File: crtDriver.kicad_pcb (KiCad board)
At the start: 2 copper layers, 29 parts, among them J1 Lum_In, J2 V_Sync, J3 H_Sync, Q1 2N7000, Q2 2N7000, Q3 2N7000, Q4 2N7000

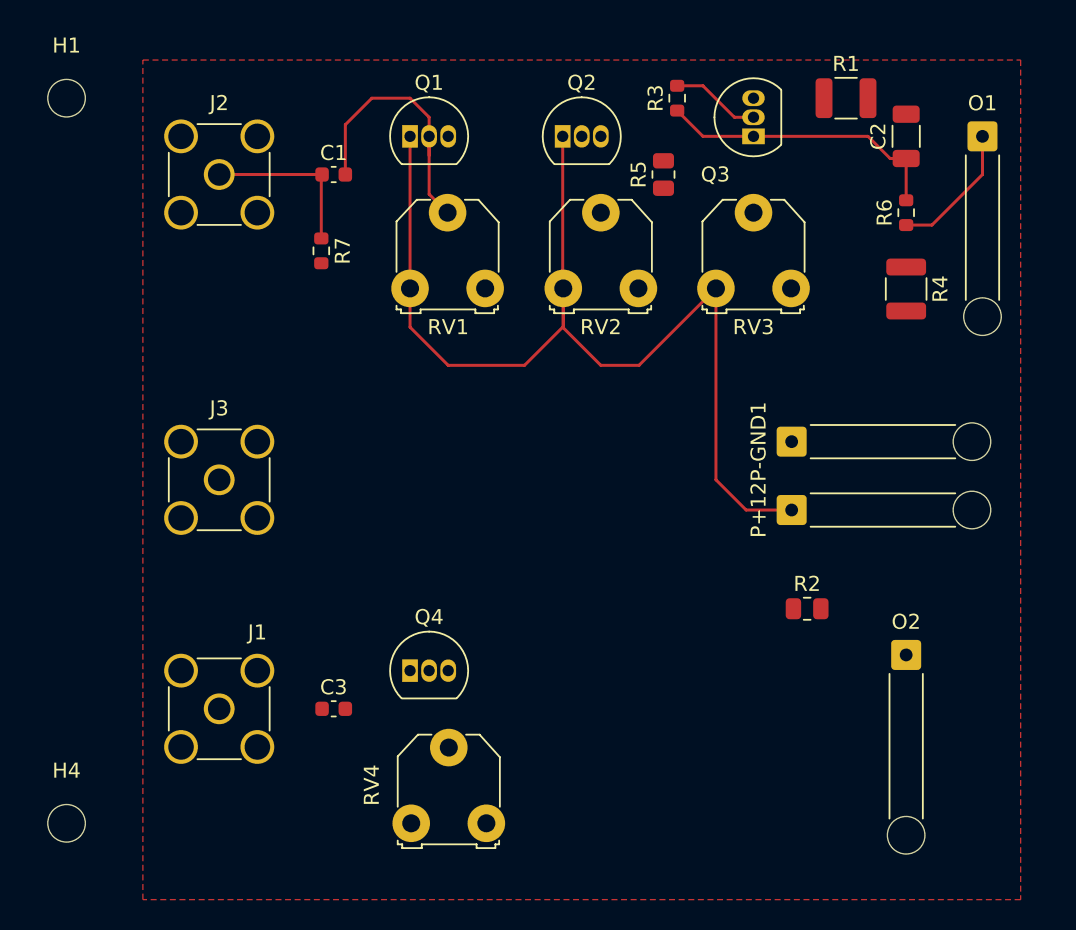
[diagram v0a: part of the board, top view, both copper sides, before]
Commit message: changed circuit to use 2n7000's as low side switches/valves to get voltage gain, started on current mirror for linear capacitor voltage ramp (it also will likely only work on the low side maybe requiring inverting of the fill/drain modes/roles, fixed luminosity amplifier design by also using mosfet on low(-) side of a resistor to boost the voltage of the input signal
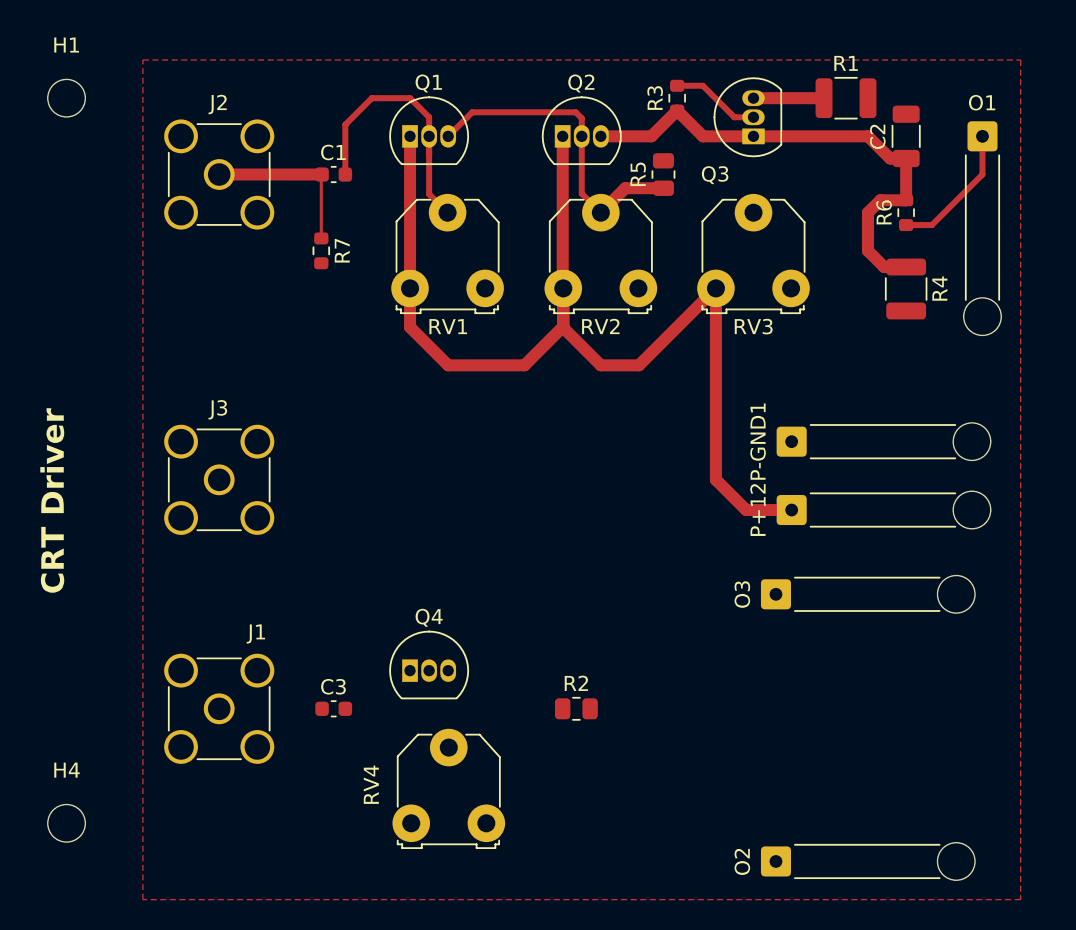
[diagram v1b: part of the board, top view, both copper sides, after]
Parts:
- added O3: V_Ramp_Out, Connector_Wire:SolderWire-0.25sqmm_1x01_D0.65mm_OD2mm_Relief, F.Cu at (151.4, 53.3)
- moved R2 16.7 mm to (138.1, 61.0)
- moved O2 16.2 mm to (151.4, 71.1), turned to 90 degrees
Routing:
- net Net-(Q1-D): track 0.00 -> 21.4 mm
- net Net-(Q2-D): track 19.3 -> 33.5 mm
- net Net-(Q3-D): track 0.00 -> 4.69 mm
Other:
- board text added: "CRT Driver"

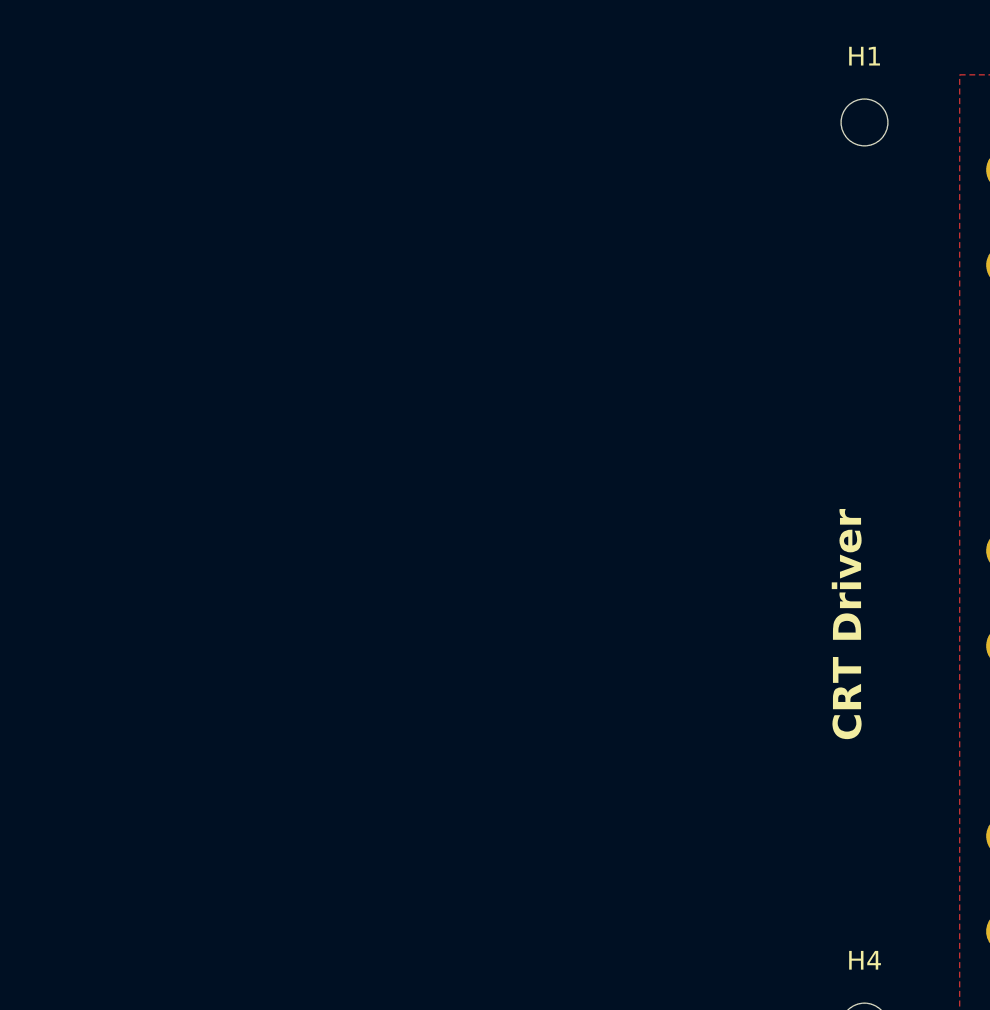
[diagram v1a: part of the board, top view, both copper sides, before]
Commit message: duplicated v sync section for h sync, adjusted luminosity amplifier passive component values
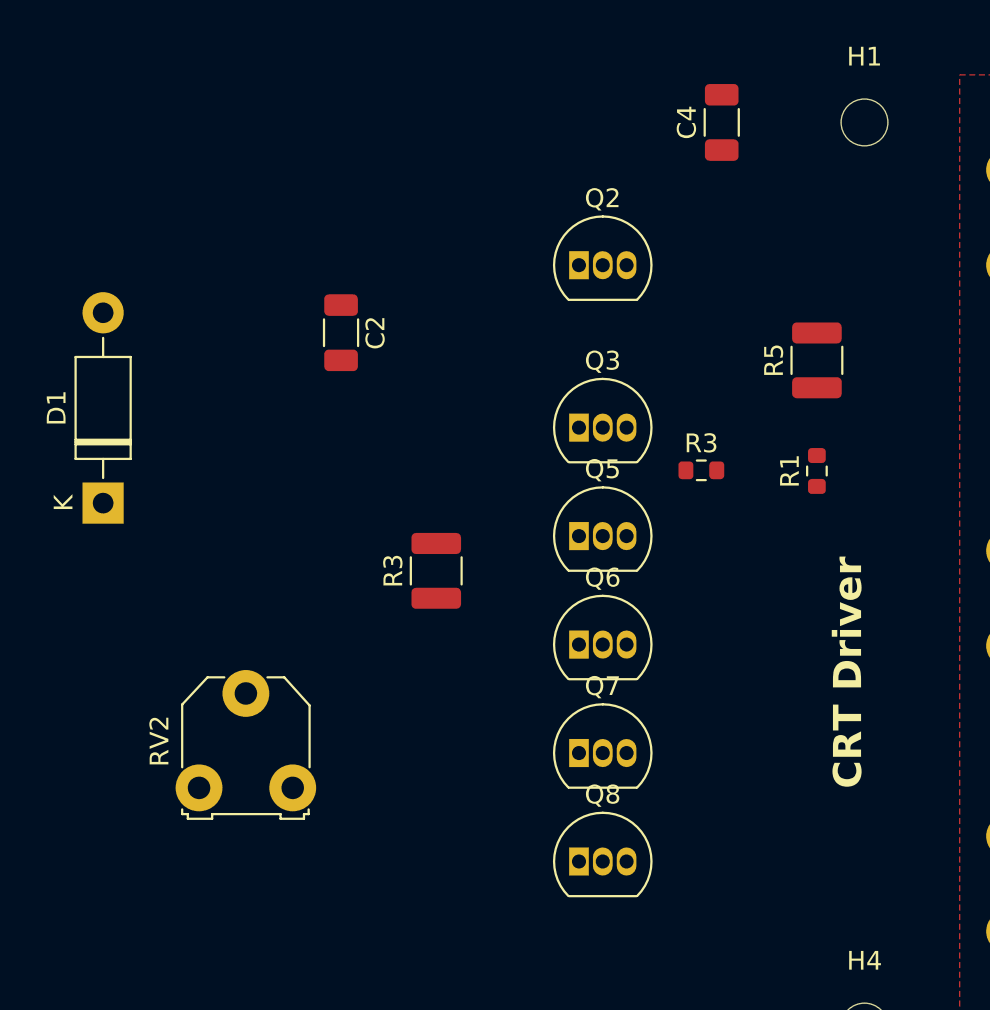
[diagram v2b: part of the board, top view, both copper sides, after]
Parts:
- added C2: 500u, Capacitor_SMD:C_1206_3216Metric, F.Cu at (76.2, 31.5)
- added C4: 47u, Capacitor_SMD:C_1206_3216Metric, F.Cu at (96.5, 20.3)
- added D1: 1N4001, Diode_THT:D_DO-41_SOD81_P10.16mm_Horizontal, F.Cu at (63.5, 40.6)
- added Q2: 2N7000, Package_TO_SOT_THT:TO-92_Inline, F.Cu at (88.9, 27.9)
- added Q3: 2N7000, Package_TO_SOT_THT:TO-92_Inline, F.Cu at (88.9, 36.6)
- added Q5: 2N7000, Package_TO_SOT_THT:TO-92_Inline, F.Cu at (88.9, 42.4)
- added Q6: 2N7000, Package_TO_SOT_THT:TO-92_Inline, F.Cu at (88.9, 48.2)
- added Q7: 2N7000, Package_TO_SOT_THT:TO-92_Inline, F.Cu at (88.9, 54.0)
- added Q8: 2N7000, Package_TO_SOT_THT:TO-92_Inline, F.Cu at (88.9, 59.8)
- added R1: 10000, Resistor_SMD:R_0603_1608Metric, F.Cu at (101.6, 38.9)
- added R3: 68, Resistor_SMD:R_0603_1608Metric, F.Cu at (95.4, 38.9)
- added R3: 10, Resistor_SMD:R_1210_3225Metric, F.Cu at (81.3, 44.3)
- added R5: 1000, Resistor_SMD:R_1210_3225Metric, F.Cu at (101.6, 33.0)
- added RV2: 250, crtDriver:Potentiometer_Triwood_RM-065, F.Cu at (68.6, 55.8)
- C3: value 10n -> 100n
- R2: value 1000 -> 100000
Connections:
- C3 pad 2: GND -> Net-(Q4-G)
- O2 pad 1: Net-(Q4-D) -> Net-(Q4-S)
- Q1 pad 1: +12V -> /Inverted V Sync
- Q1 pad 3: Net-(Q1-D) -> GND
- Q4 pad 1: +12V -> Net-(Q4-S)
- Q4 pad 2: Net-(J1-In) -> Net-(Q4-G)
- Q4 pad 3: Net-(Q4-D) -> GND
- R2 pad 1: Net-(Q4-D) -> +12V
- R2 pad 2: GND -> Net-(Q4-S)
- RV4 pad 2: Net-(J1-In) -> Net-(Q4-G)

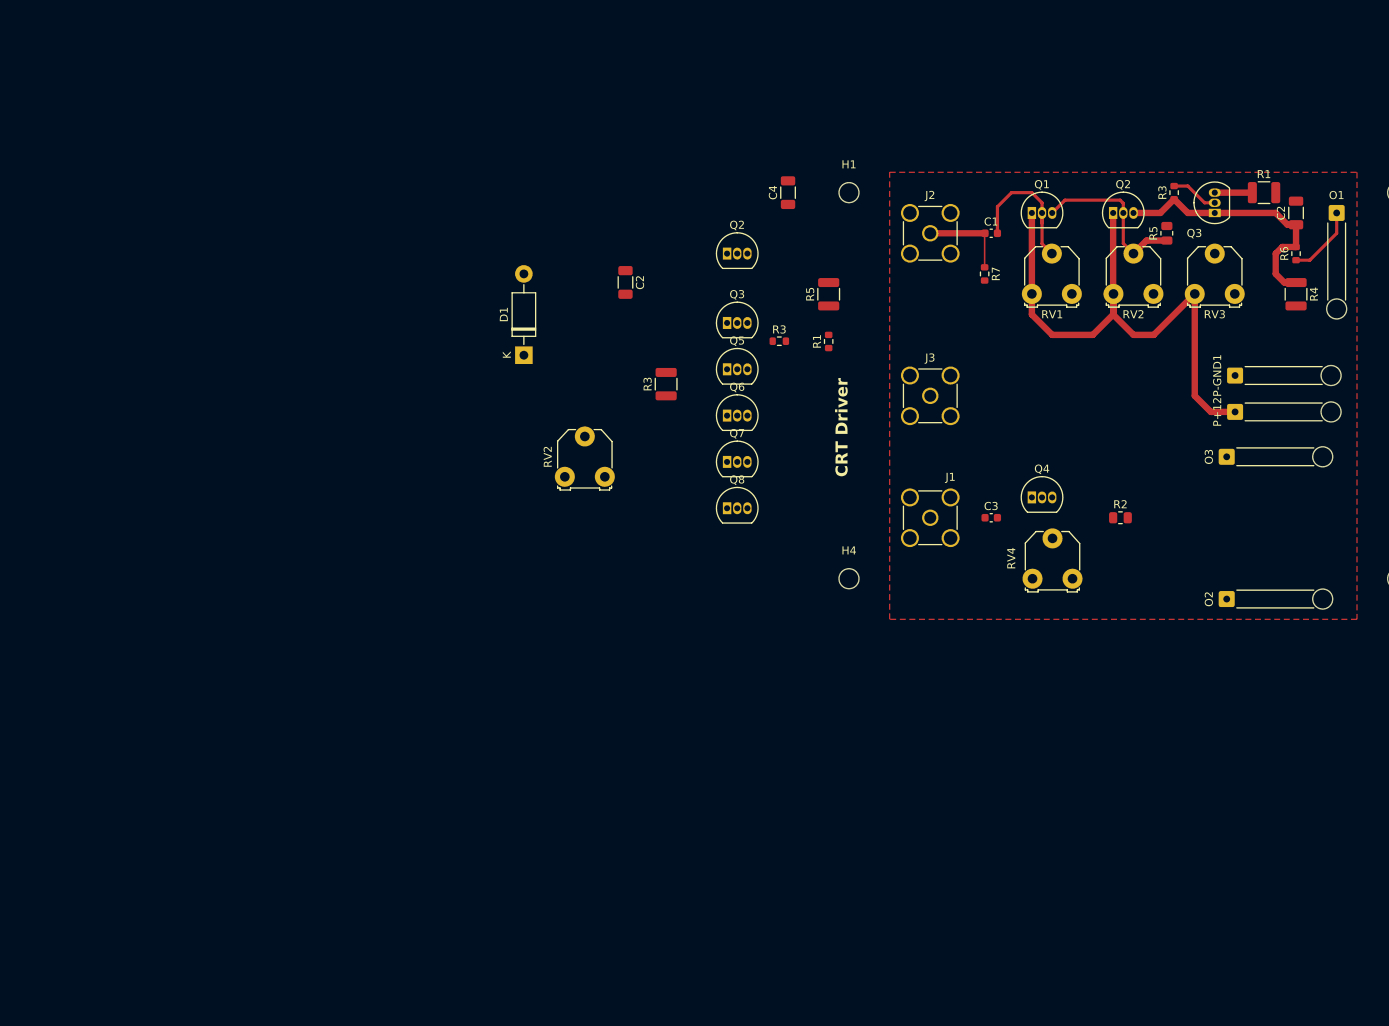
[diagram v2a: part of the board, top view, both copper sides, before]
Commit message: updated schematic with voltage booster section, haven't found settings for it to be simulated stabily in spice without many iterations/timesteps yet
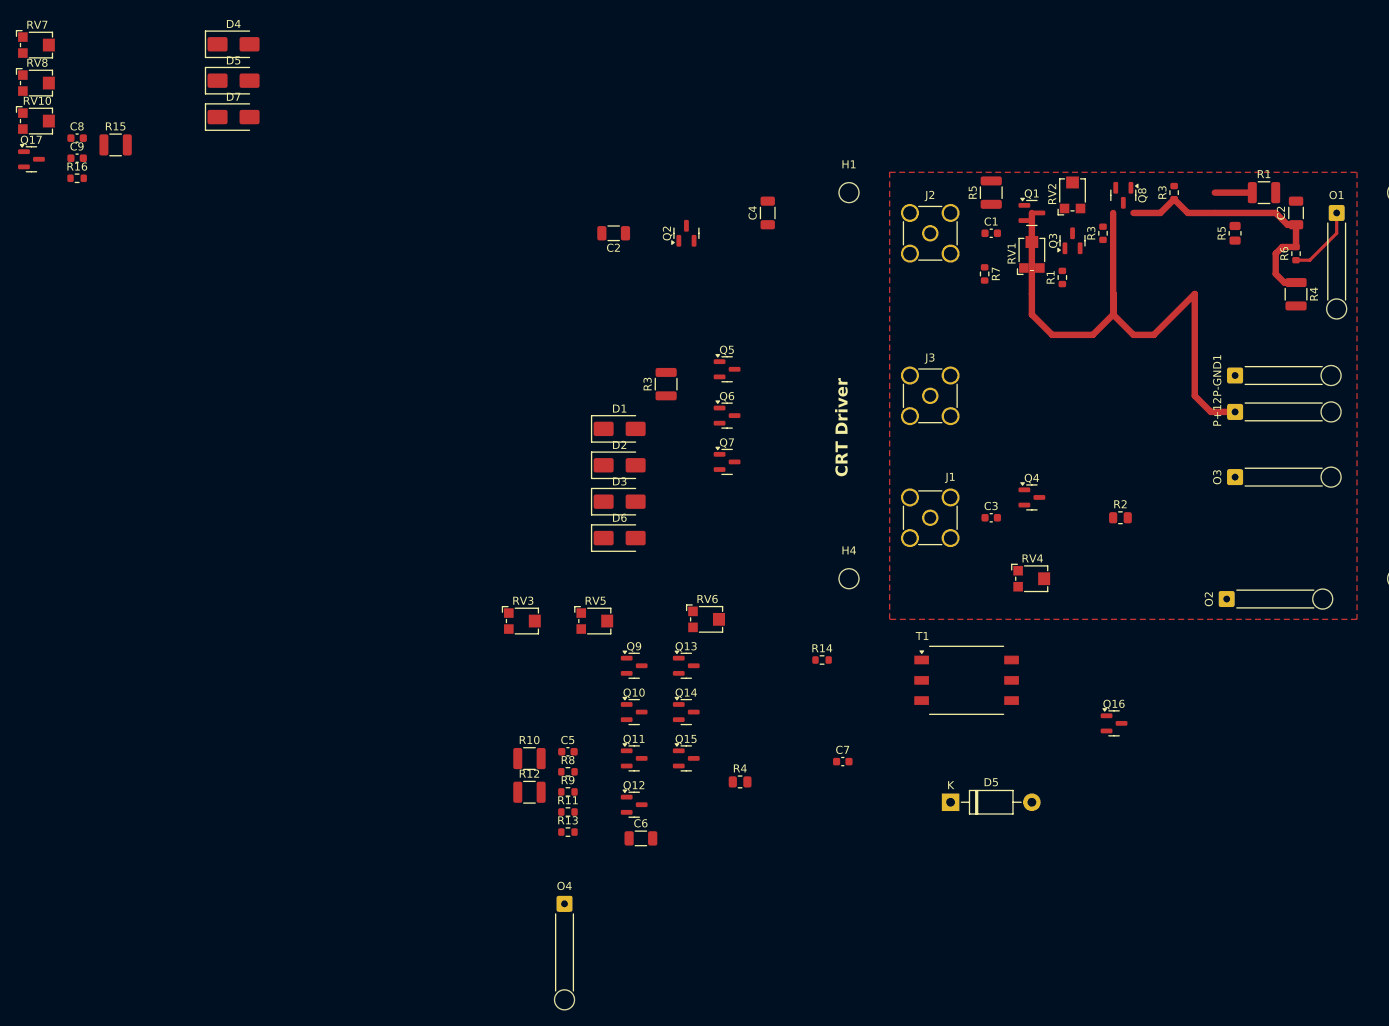
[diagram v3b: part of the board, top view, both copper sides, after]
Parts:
- removed the Q2 at (137.2, 22.9)
- removed the Q3 at (149.9, 22.9)
- removed the RV2 at (137.2, 33.0)
- added C5: 4u, Capacitor_SMD:C_0603_1608Metric, F.Cu at (69.0, 90.2)
- added C6: 47u, Capacitor_SMD:C_1206_3216Metric, F.Cu at (78.1, 101.0)
- added C7: 20u, Capacitor_SMD:C_0603_1608Metric, F.Cu at (103.4, 91.4)
- added C8: 4u, Capacitor_SMD:C_0603_1608Metric, F.Cu at (7.66, 13.5)
- added C9: 1u, Capacitor_SMD:C_0603_1608Metric, F.Cu at (7.66, 16.0)
- added D2: US1A, Diode_SMD:D_SMA, F.Cu at (75.5, 54.4)
- added D3: US1A, Diode_SMD:D_SMA, F.Cu at (75.5, 59.0)
- added D4: US1A, Diode_SMD:D_SMA, F.Cu at (27.2, 1.77)
- added D5: US1A, Diode_SMD:D_SMA, F.Cu at (27.2, 6.33)
- added D5: 1N4007, Diode_THT:D_DO-41_SOD81_P10.16mm_Horizontal, F.Cu at (116.8, 96.5)
- added D6: US1A, Diode_SMD:D_SMA, F.Cu at (75.5, 63.5)
- added D7: US1A, Diode_SMD:D_SMA, F.Cu at (27.2, 10.9)
- added O4: V_Ramp_Out, Connector_Wire:SolderWire-0.25sqmm_1x01_D0.65mm_OD2mm_Relief, F.Cu at (68.6, 109.2)
- added Q10: 2N7000, Package_TO_SOT_SMD:SOT-23, F.Cu at (77.3, 85.2)
- added Q11: 2N7000, Package_TO_SOT_SMD:SOT-23, F.Cu at (77.3, 91.0)
- added Q12: 2N7000, Package_TO_SOT_SMD:SOT-23, F.Cu at (77.3, 96.8)
- added Q13: 2N7000, Package_TO_SOT_SMD:SOT-23, F.Cu at (83.8, 79.5)
- added Q14: 2N7000, Package_TO_SOT_SMD:SOT-23, F.Cu at (83.8, 85.2)
- added Q15: 2N7000, Package_TO_SOT_SMD:SOT-23, F.Cu at (83.8, 91.0)
- added Q16: 2N7000, Package_TO_SOT_SMD:SOT-23, F.Cu at (137.3, 86.7)
- added Q17: 2N7000, Package_TO_SOT_SMD:SOT-23, F.Cu at (1.95, 16.1)
- added Q9: 2N7000, Package_TO_SOT_SMD:SOT-23, F.Cu at (77.3, 79.5)
- added R10: 1000, Resistor_SMD:R_1210_3225Metric, F.Cu at (64.2, 91.1)
- added R11: 10000, Resistor_SMD:R_0603_1608Metric, F.Cu at (69.0, 97.7)
- added R12: 10, Resistor_SMD:R_1210_3225Metric, F.Cu at (64.2, 95.3)
- added R13: 1000, Resistor_SMD:R_0603_1608Metric, F.Cu at (69.0, 100.2)
- added R14: 10000, Resistor_SMD:R_0603_1608Metric, F.Cu at (100.8, 78.7)
- added R15: .5, Resistor_SMD:R_1210_3225Metric, F.Cu at (12.5, 14.4)
- added R16: .5, Resistor_SMD:R_0603_1608Metric, F.Cu at (7.66, 18.5)
- added R4: 100, Resistor_SMD:R_0805_2012Metric, F.Cu at (90.5, 94.0)
- added R8: 10000, Resistor_SMD:R_0603_1608Metric, F.Cu at (69.0, 92.7)
- added R9: 1000000, Resistor_SMD:R_0603_1608Metric, F.Cu at (69.0, 95.2)
- added RV10: 2000, Potentiometer_SMD:Potentiometer_Bourns_TC33X_Vertical, F.Cu at (2.67, 11.4)
- added RV5: 2M, Potentiometer_SMD:Potentiometer_Bourns_TC33X_Vertical, F.Cu at (72.5, 73.9)
- added RV6: 5000, Potentiometer_SMD:Potentiometer_Bourns_TC33X_Vertical, F.Cu at (86.4, 73.7)
- added RV7: 2000, Potentiometer_SMD:Potentiometer_Bourns_TC33X_Vertical, F.Cu at (2.67, 1.88)
- added RV8: 2000, Potentiometer_SMD:Potentiometer_Bourns_TC33X_Vertical, F.Cu at (2.67, 6.62)
- added T1: Transformer_1P_1S, Transformer_SMD:Transformer_Wuerth_750315371, F.Cu at (118.8, 81.3)
- D1: value 1N4001 -> US1A; footprint Diode_THT:D_DO-41_SOD81_P10.16mm_Horizontal -> Diode_SMD:D_SMA
- J2: value V_Sync -> H_Sync
- J3: value H_Sync -> V_Sync
- Q1, Q2, Q3, Q4, Q5, Q6, Q7, Q8: footprint Package_TO_SOT_THT:TO-92_Inline -> Package_TO_SOT_SMD:SOT-23
- RV1, RV2, RV4: footprint crtDriver:Potentiometer_Triwood_RM-065 -> Potentiometer_SMD:Potentiometer_Bourns_TC33X_Vertical
- RV3: value 10M -> 2000; footprint crtDriver:Potentiometer_Triwood_RM-065 -> Potentiometer_SMD:Potentiometer_Bourns_TC33X_Vertical
- moved RV3 93.4 mm to (63.4, 73.9)
- moved RV2 72.6 mm to (132.1, 20.5), turned to 90 degrees
- moved Q8 63.1 mm to (138.4, 20.7), turned to -90 degrees
- moved Q3 44.4 mm to (132.1, 26.3), turned to 90 degrees
- moved R3 42.6 mm to (135.9, 25.4), turned to 90 degrees
- moved R1 30.3 mm to (130.8, 30.9)
- moved R5 24.0 mm to (121.9, 20.3)
- moved D1 15.1 mm to (75.5, 49.9), turned to 0 degrees
- moved R5 8.53 mm to (152.4, 25.4)
- moved C2 6.32 mm to (74.7, 25.4), turned to 180 degrees
- moved Q2 5.68 mm to (83.8, 25.4), turned to 90 degrees
- moved RV1 5.04 mm to (127.0, 27.9), turned to 90 degrees
- moved C4 3.59 mm to (94.0, 22.9)
- moved O3 2.75 mm to (152.4, 55.9)
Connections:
- net /Inverted V Sync renamed /Inverted H Sync
- net /Positive V Sync renamed /Positive H Sync
- C4 pad 1: Net-(D1-K) -> Net-(D6-K)
- C4 pad 2: Net-(Q2-D) -> Net-(D1-K)
- J3 pad 1: unconnected-(J3-In-Pad1) -> Net-(J3-In)
- O2 pad 1: Net-(Q4-S) -> Net-(O2-Pad1)
- Q2 pad 3: Net-(Q2-D) -> Net-(D1-A)
- Q5 pad 1: Net-(D1-K) -> Net-(D6-K)
- Q7 pad 1: Net-(Q2-D) -> Net-(D1-K)
- Q8 pad 3: Net-(D1-A) -> Net-(D6-A)
- R2 pad 2: Net-(Q4-S) -> Net-(R2-Pad2)
- R6 pad 2: Net-(Q2-D) -> Net-(D1-K)
- RV2 pad 1: Net-(D1-A) -> Net-(D6-A)
- RV3 pad 1: +12V -> Net-(R4-Pad2)
- RV3 pad 2: Net-(Q3-G) -> Net-(Q4-S)
- RV3 pad 3: GND -> Net-(R2-Pad2)
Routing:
- net Net-(Q1-D): track 21.4 -> 0.00 mm
- net Net-(Q1-G): track 18.3 -> 0.00 mm
- net Net-(J2-In): track 11.1 -> 0.00 mm
- net Net-(Q3-G): track 5.95 -> 0.00 mm
